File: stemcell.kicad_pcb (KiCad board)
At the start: 4 copper layers, 17.8 x 31.9 mm, 35 parts, among them J1 USB C Connector, J2 Left, J3 Right, J4 Down, SW1 Boot0, U1 STM32F401RCTx, U2 XC6220B331MR, Y1 HSE1 8Mhz 12pF

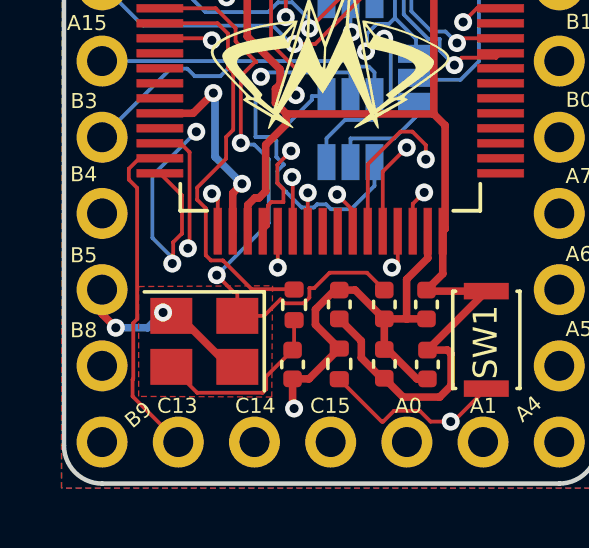
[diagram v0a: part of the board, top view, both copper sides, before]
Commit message: Move via out of the crystal zone.
Regenerated the gerbers.
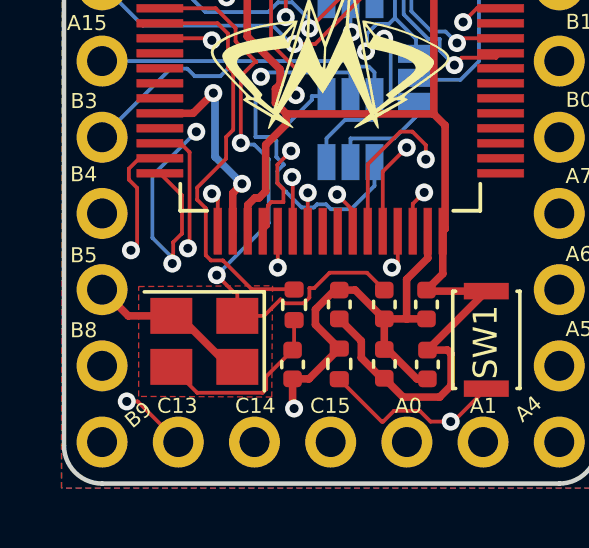
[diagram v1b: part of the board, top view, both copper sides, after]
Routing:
- net GND: track 82.0 -> 102.4 mm, vias 6 -> 4
- net /RX0: track 39.4 -> 41.3 mm
- net /PA1: track 11.1 -> 11.6 mm, vias 0 -> 2

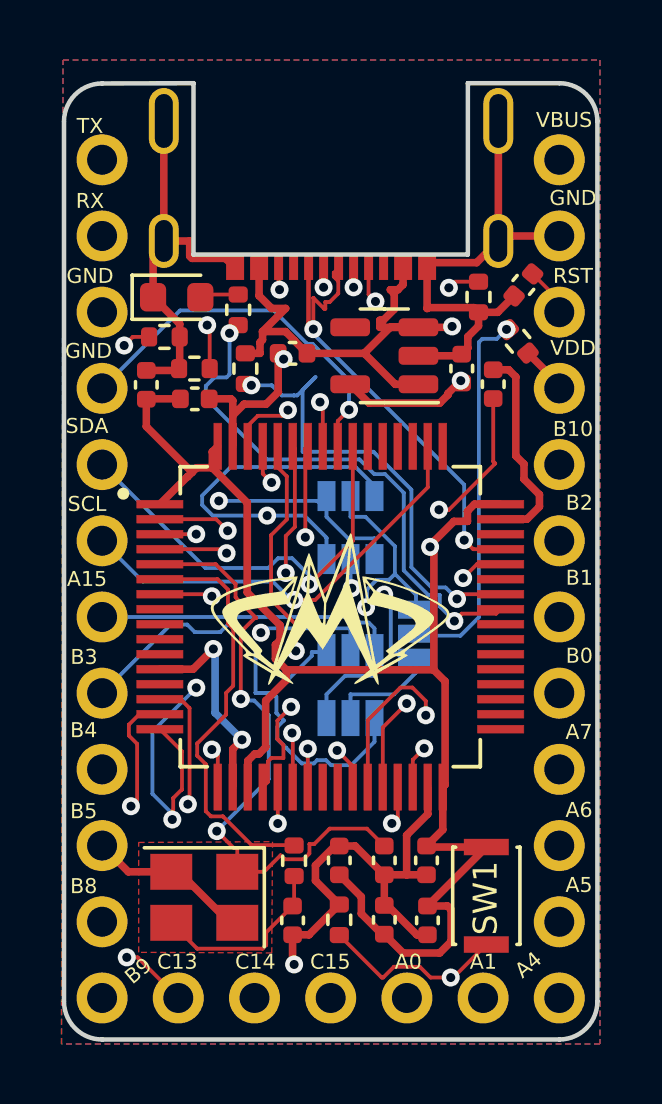
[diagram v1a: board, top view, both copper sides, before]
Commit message: Moved capacitors out of the way of the pins
Moved logo back to the back silkscreen.
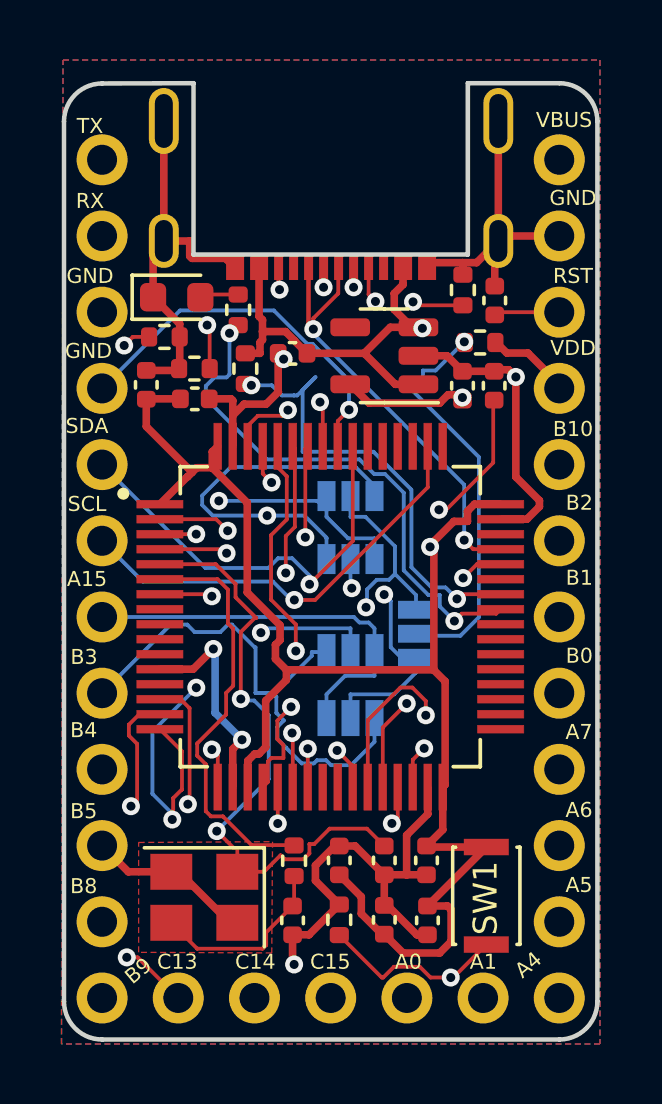
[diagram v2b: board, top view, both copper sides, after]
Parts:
- G***: moved to B.Cu
- moved G*** 7.75 mm to (97.9, 74.2), turned to 180 degrees
- moved R7 1.27 mm to (105.1, 57.9), turned to 180 degrees
- moved C12 1.08 mm to (105.6, 56.5), turned to 90 degrees
- moved C2 0.57 mm to (104.5, 59.3)
- moved R2 0.57 mm to (104.5, 56.1), turned to 90 degrees
- moved C3 0.06 mm to (105.6, 59.3)
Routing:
- net VDD: track 66.6 -> 68.6 mm
- net GND: track 102.4 -> 104.2 mm, vias 4 -> 5
- net /USB_DP: track 15.9 -> 15.0 mm
- net VBUS: track 24.7 -> 23.9 mm
- net /TX_PULLUP: track 12.7 -> 13.5 mm
- net /CC1: track 4.92 -> 4.18 mm
- net /NRST: track 18.9 -> 19.6 mm
